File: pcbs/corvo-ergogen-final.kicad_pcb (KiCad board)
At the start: 2 copper layers, 135 x 94.5 mm, 87 parts

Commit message: final pcb v1
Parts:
- moved RE1 1.81 mm to (252.5, 132.4)
- moved D25 1.55 mm to (248.5, 136.5)
- moved TRRS1 1.11 mm to (263.5, 144.3)
- moved PWR1 1.01 mm to (262.5, 125.6)
- moved RST1 0.51 mm to (262.0, 135.0)
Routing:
- net P10: track 104.5 -> 264.0 mm, vias 4 -> 7
- net P0: track 109.9 -> 241.7 mm, vias 4 -> 6
- net P2: track 104.8 -> 200.3 mm, vias 4 -> 6
- net P6: track 144.7 -> 214.9 mm
- net P3: track 129.9 -> 198.7 mm, vias 4 -> 6
- net P4: track 119.4 -> 164.9 mm, vias 4 -> 5
- net P9: track 108.5 -> 153.0 mm
- net GND: track 168.1 -> 207.3 mm, vias 44 -> 70
- net P7: track 132.2 -> 161.0 mm
- net P8: track 108.6 -> 135.7 mm, vias 0 -> 2
- net VCC: track 705.6 -> 680.6 mm
- net P5: track 115.8 -> 132.8 mm, vias 4 -> 5
- net P15: track 61.9 -> 59.3 mm
- net encoder: track 11.4 -> 13.3 mm
- net P1: track 42.8 -> 41.0 mm
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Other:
- board size 135 x 94.5 mm -> 135.9 x 94.5 mm

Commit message: updated final pcb
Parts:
- moved MH2 2.31 mm to (260.0, 152.1)
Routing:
- net P1: track 41.0 -> 42.3 mm
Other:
- outline, holes or cut-outs redrawn
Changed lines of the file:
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@@
 			(outputformat 1)
 			(mirror no)
-			(drillshape 1)
+			(drillshape 0)
 			(scaleselection 1)
-			(outputdirectory "")
+			(outputdirectory "gerber-final-v1")
 		)
 	)
@@
 	(footprint "ceoloide:mounting_hole_npth"
 		(layer "F.Cu")
-		(at 257.894133 151.14426)
+		(at 260 152.1)
 		(property "Reference" "MH2"
 			(at 0 2.55 0)
@@
 	)
 	(gr_line
-		(start 264 152)
-		(end 264 88)
+		(start 264 151.95)
+		(end 264 88.925)
 		(stroke
 			(width 0.15)
@@
 		(layer "Edge.Cuts")
 	)
-	(gr_line
-		(start 264 87)
-		(end 262.094133 86.76926)
-		(stroke
-			(width 0.15)
-			(type default)
-		)
-		(layer "Edge.Cuts")
-	)
 	(gr_arc
 		(start 183.094133 82.91926)
@@
 	)
 	(gr_line
-		(start 264 88)
-		(end 264 87)
-		(stroke
-			(width 0.2)
-			(type default)
-		)
-		(layer "Edge.Cuts")
-	)
-	(gr_line
 		(start 231.942053 166.079842)
 		(end 214.822962 161.492794)
@@
 	)
 	(gr_line
+		(start 264 88.675)
+		(end 264 88.925)
+		(stroke
+			(width 0.15)
+			(type default)
+		)
+		(layer "Edge.Cuts")
+	)
+	(gr_line
 		(start 167.094133 160.56926)
 		(end 129.094133 160.56926)
@@
 	)
 	(gr_line
-		(start 264 152)
+		(start 264 151.95)
 		(end 250.14675 176.009203)
 		(stroke
@@
 		(layer "Edge.Cuts")
 	)
+	(gr_arc
+		(start 262.094073 86.775009)
+		(mid 263.441406 87.329403)
+		(end 264 88.675)
+		(stroke
+			(width 0.15)
+			(type default)
+		)
+		(layer "Edge.Cuts")
+	)
 	(segment
 		(start 247.919133 89.329259)
@@
 	)
 	(segment
+		(start 249.094134 90.504259)
+		(end 247.719134 90.504259)
+		(width 0.2)
+		(layer "F.Cu")
+		(net 1)
+	)
+	(segment
 		(start 244.387433 89.329259)
 		(end 247.919133 89.329259)
@@
 		(width 0.2)
 		(layer "B.Cu")
-		(net 12)
-	)
-	(segment
-		(start 233.311764 88.188236)
-		(end 233.30378 88.180251)
-		(width 0.2)
-		(layer "B.Cu")

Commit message: updated final pcb w/ gerbers
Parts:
- moved PWR1 0.26 mm to (262.2, 125.6)
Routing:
- net rgb: track 879.5 -> 838.9 mm
- net GND: track 207.3 -> 243.2 mm, vias 70 -> 85
- net VCC: track 680.6 -> 707.7 mm, vias 49 -> 52
- net P14: track 37.8 -> 39.7 mm
- net P9: track 153.0 -> 154.1 mm
- net RST: track 64.8 -> 65.6 mm
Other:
- board text added: "corvo - theb0b 8/25/26"

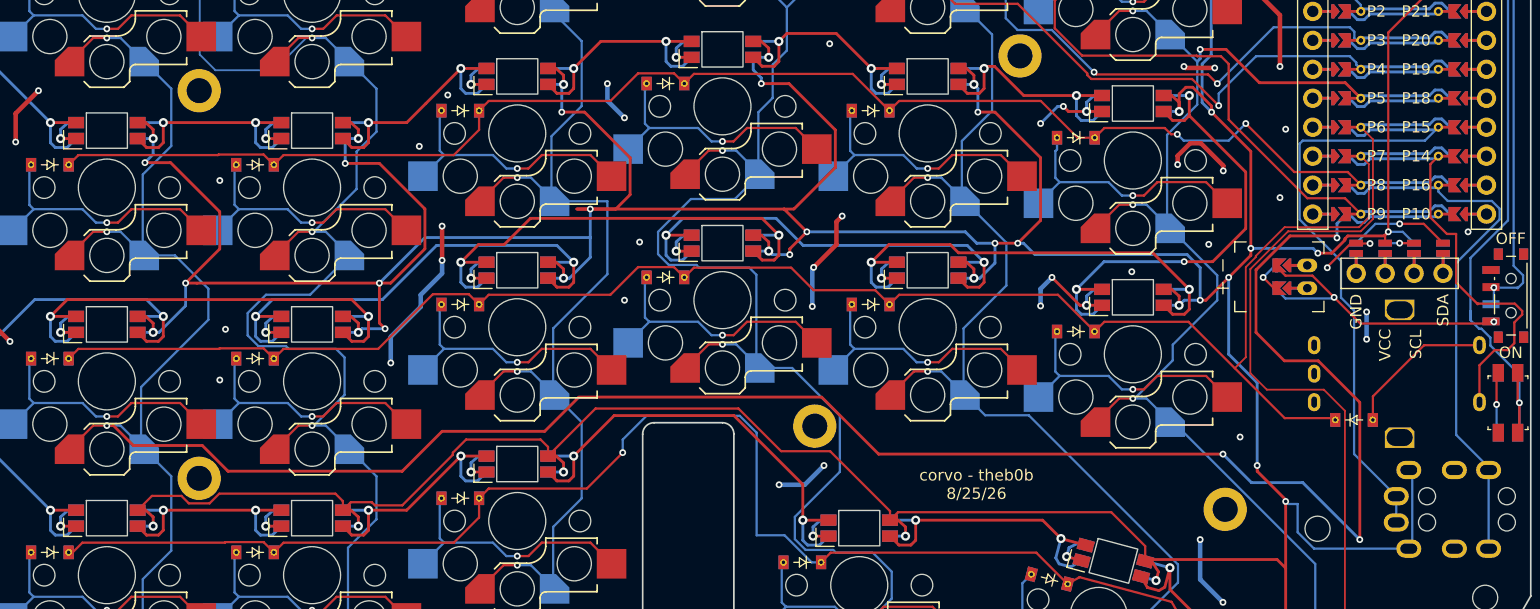
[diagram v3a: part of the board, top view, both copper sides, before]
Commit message: updated pcb to have spin support for the encoders
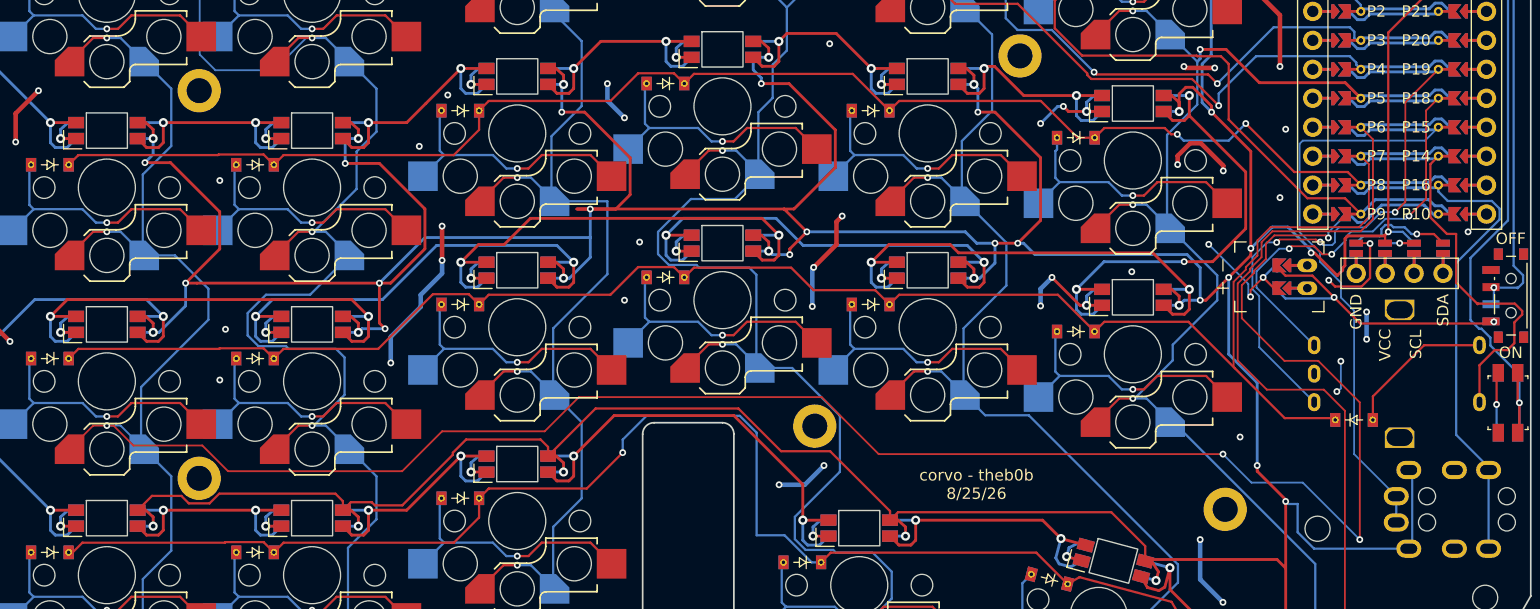
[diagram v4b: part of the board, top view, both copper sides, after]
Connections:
- RE1 pad A: RE_A -> P19
- RE1 pad C: RE_C -> P18
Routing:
- net P19: track 9.83 -> 54.0 mm, vias 0 -> 3
- net P18: track 9.83 -> 45.9 mm, vias 0 -> 3
- net GND: track 243.2 -> 258.1 mm, vias 85 -> 88
- net VCC: track 707.7 -> 712.4 mm
- net P10: track 263.9 -> 266.2 mm
- net P6: track 214.8 -> 216.5 mm
- net P7: track 161.0 -> 161.8 mm
- net RST: track 65.6 -> 64.8 mm
